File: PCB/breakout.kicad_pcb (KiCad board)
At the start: 2 copper layers, 25.4 x 17.8 mm, 20 parts, among them J1 BKOUT_PINS, J2 POTENTIOMETER, U1 AD5293

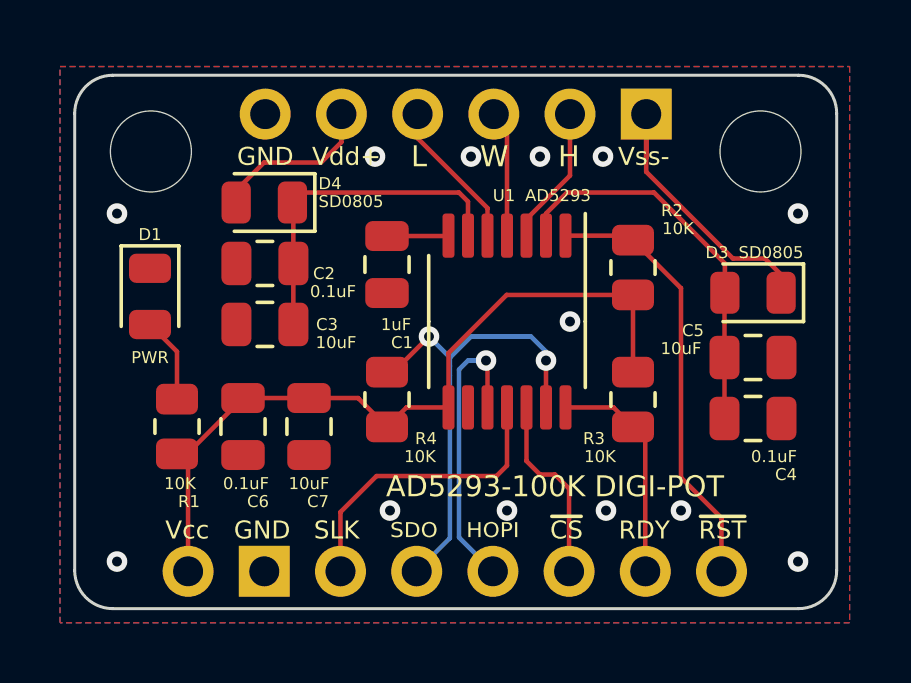
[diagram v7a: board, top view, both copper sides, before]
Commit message: update design; add SDO pull-up jumper
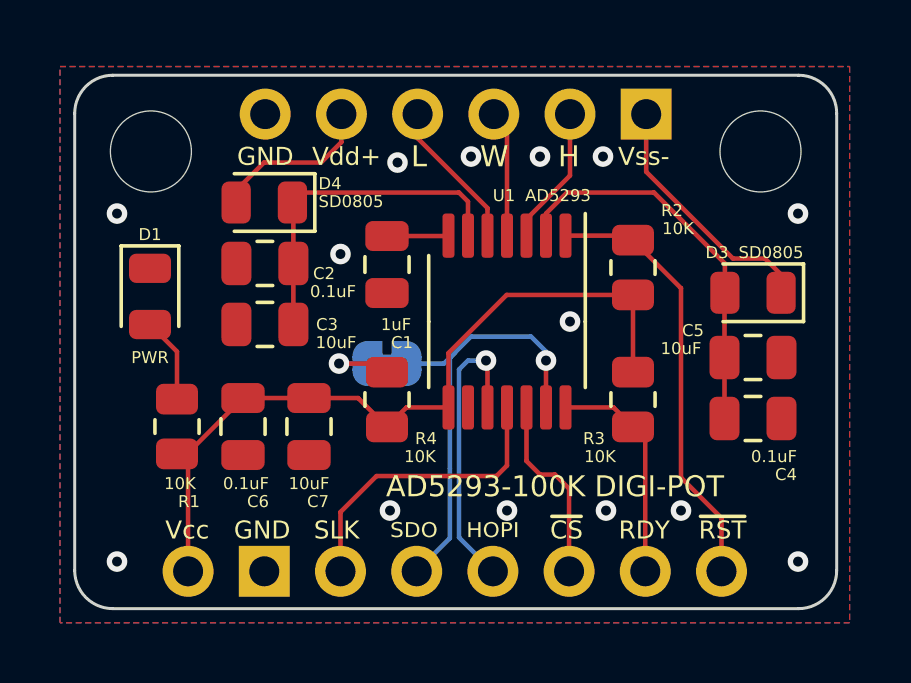
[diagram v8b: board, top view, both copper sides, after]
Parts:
- added JP1: SDO PULL-UP, Jumper:SolderJumper-2_P1.3mm_Bridged_RoundedPad1.0x1.5mm, B.Cu at (146.3, 107.4)
- moved G*** 10.5 mm to (153.4, 102.8)
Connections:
- R4 pad 2: /SDO -> Net-(JP1-Pad1)
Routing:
- net Net-(JP1-Pad1): track 0.00 -> 2.67 mm, vias 0 -> 1
- net Net-(D3-Pad1): track 9.92 -> 8.44 mm
- net /SDO: track 16.2 -> 14.9 mm, vias 2 -> 1
- net GND: vias 13 -> 14
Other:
- board text added: "2023-04-20 2.0.2"
- board text removed: "2023-03-25 2.0.1"
